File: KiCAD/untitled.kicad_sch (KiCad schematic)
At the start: 71 parts, among them J1 Power, J10 Conn_01x04, J11 Conn_01x04, J12 FDCAN_1, J13 FDCAN_2, J5 Debug Header, J6 Conn_01x04, J7 Conn_01x04, J8 Conn_01x04, J9 Conn_01x04, Q6 AO3400A, Q7 AO3400A, Q8 AO3400A, SW1 PTS810SJM250SMTRLFS, SW2 PTS810SJM250SMTRLFS, SW3 PTS810SJM250SMTRLFS, SW4 PTS810SJM250SMTRLFS, SW5 SMQS-02R-TP, U1 STM32H573RIT6, U12 TPS7A2033DQNR, U5 USBLC6-2SC6, U7 MCP2562FD-E/P, U8 MCP2562FD-E/P, X1 SC-32S32.768kHz20PPM7pF, Y2 ECS-80-18-23B-JTM-TR

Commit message: Sync KiCAD project
Forgot to push this earlier
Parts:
- C11: LCSC Part (none) -> C19666
- C12, C13, C14, C15, C17, C26, C27, C30, C8: LCSC Part (none) -> C1525
- C16: LCSC Part (none) -> C15849
- C22: LCSC Part (none) -> C440198
- C23, C28, C29: LCSC Part (none) -> C307331
- C24: LCSC Part (none) -> C52923
- C25: LCSC Part (none) -> C23630
- D5: LCSC Part (none) -> C2297
- D6: LCSC Part (none) -> C2296
- R14, R15, R24, R26, R28: LCSC Part (none) -> C25744
- R16, R17: LCSC Part (none) -> C25905
- R18: LCSC Part (none) -> C22775
- R19: LCSC Part (none) -> C22962
- R20, R21: LCSC Part (none) -> C8218
- R22: LCSC Part (none) -> C22787
- R23, R25, R27: LCSC Part (none) -> C25091
- R30, R31: LCSC Part (none) -> C17909
- U1: LCSC Part (none) -> C22371377
- U5: LCSC Part (none) -> C7519

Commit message: Fix all DRC errors
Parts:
- USBC1: footprint easyeda2kicad:USB-C_SMD-TYPE-C-31-M-12_1 -> Connector_USB:USB_C_Receptacle_HRO_TYPE-C-31-M-12
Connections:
- net GND: now also Y2.4
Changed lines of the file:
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@@
 (kicad_sch
-	(version 20250114)
+	(version 20260306)
 	(generator "eeschema")
-	(generator_version "9.0")
+	(generator_version "10.0")
 	(paper "A4")
 	(title_block

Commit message: Oscillator Test Pads + Re-Fix USB-C
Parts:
- added TP5: LSE, TestPoint:TestPoint_Pad_2.0x2.0mm, symbol Connector:TestPoint_Alt
- added TP7: HSE, TestPoint:TestPoint_Pad_2.0x2.0mm, symbol Connector:TestPoint_Alt
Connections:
- net GND: now also USBC1.2 (SH), USBC1.3 (SH), USBC1.4 (SH), USBC1.A1 (GND), USBC1.A12 (GND), USBC1.B1 (GND), USBC1.B12 (GND), USBC1.SH; no longer USBC1.A1B12 (GND), USBC1.B1A12 (GND)
- net HSE_IN: now also TP7.1
- net LSE_IN: now also TP5.1
- net USB_VBUS: now also USBC1.A4 (VBUS), USBC1.A9 (VBUS), USBC1.B4 (VBUS), USBC1.B9 (VBUS); no longer USBC1.A4B9 (VBUS), USBC1.B4A9 (VBUS)
- no-connect marks 6 -> 2
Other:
- moved on the sheet: USBC1

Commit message: USB-C Schematic Changes
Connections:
- net GND: no longer USBC1.2 (SH), USBC1.3 (SH), USBC1.4 (SH)

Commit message: Change some TPs to 2.54mm pin headers, silkscreen changes, start led redo
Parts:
- added D10: SK6812MINI-E, LED_SMD:LED_SK6812MINI-E_3.2x2.8mm_P1.5mm_ReverseMount, symbol LED:SK6812MINI-E

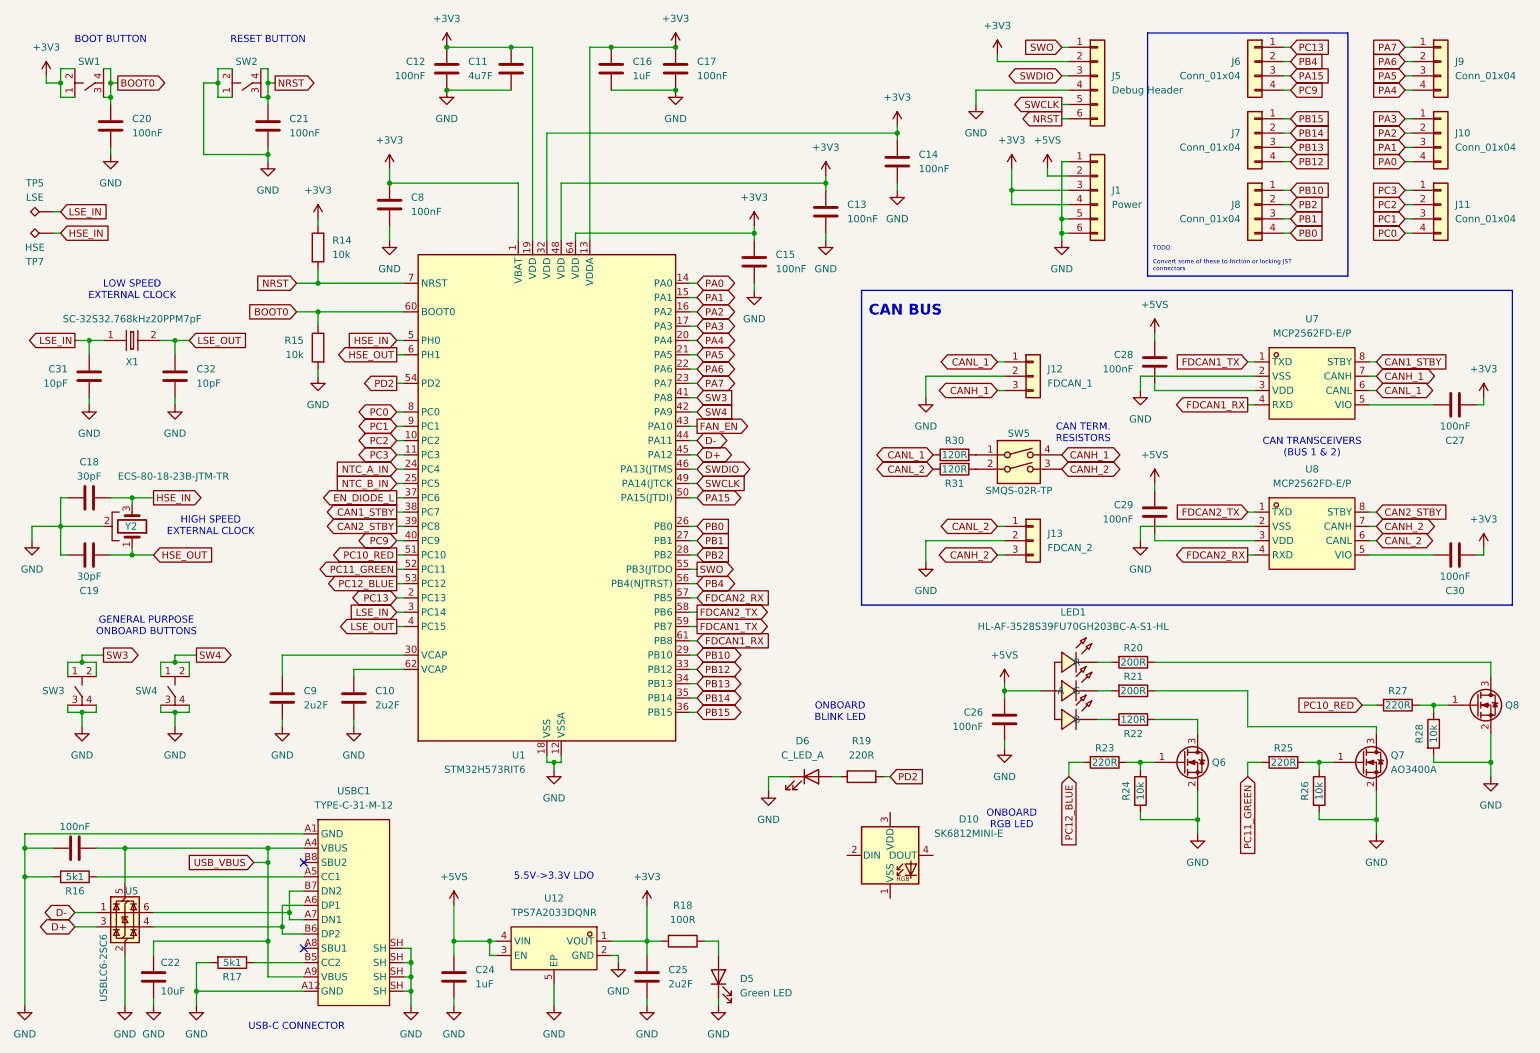
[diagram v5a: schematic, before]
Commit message: Replace RGB LED with cheaper SK6812 LEDs, expose freed UART pins
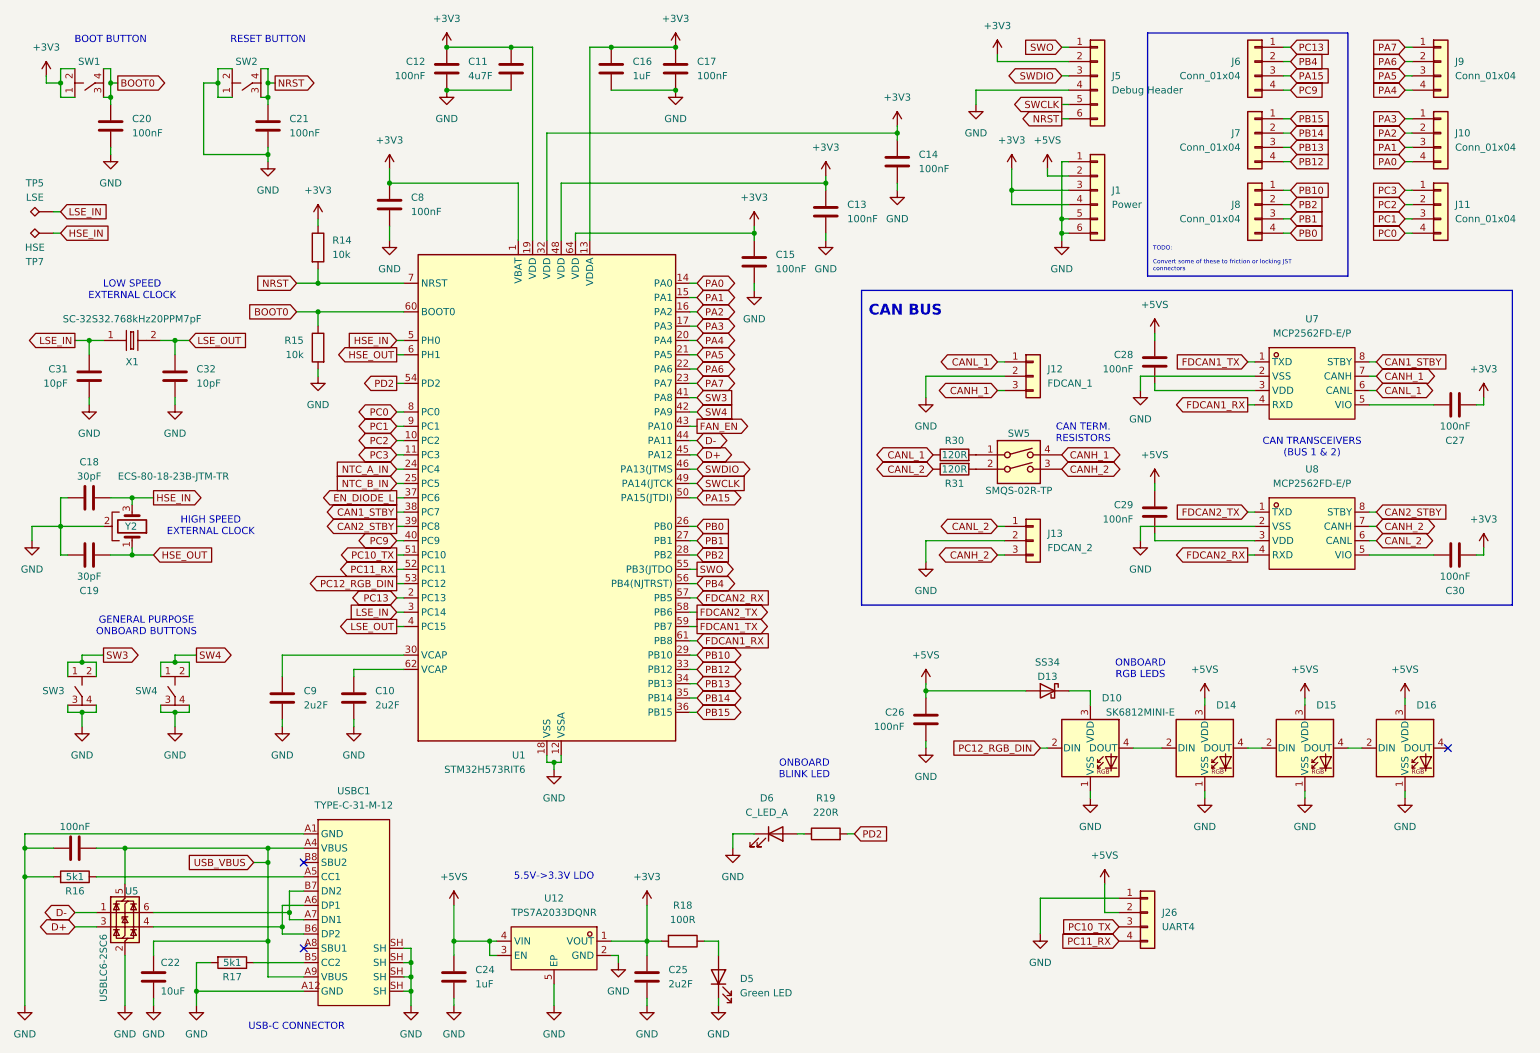
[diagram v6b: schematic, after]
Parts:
- removed LED1: HL-AF-3528S39FU70GH203BC-A-S1-HL, easyeda2kicad:LED-SMD_4P-L3.2-W2.7-TL_HL-AF-3528S39FU70GH20, symbol easyeda2kicad:HL-AF-3528S39FU70GH203BC-A-S1-HL
- removed Q6, Q7, Q8: AO3400A, Package_TO_SOT_SMD:SOT-23, symbol Transistor_FET:AO3400A
- removed R20, R21: 200R, Resistor_SMD:R_0603_1608Metric, symbol Device:R
- removed R22: 120R, Resistor_SMD:R_0603_1608Metric, symbol Device:R
- removed R23, R25, R27: 220R, Resistor_SMD:R_0402_1005Metric, symbol Device:R
- removed R24, R26, R28: 10k, Resistor_SMD:R_0402_1005Metric, symbol Device:R
- added D13: SS34, Diode_SMD:D_SMA, symbol Device:D_Schottky
- added D14, D15, D16: SK6812MINI-E, LED_SMD:LED_SK6812MINI-E_3.2x2.8mm_P1.5mm_ReverseMount, symbol LED:SK6812MINI-E
- added J26: UART4, Connector_PinHeader_2.54mm:PinHeader_1x04_P2.54mm_Vertical, symbol Connector_Generic:Conn_01x04
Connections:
- net PC12_BLUE is gone; now on net PC12_RGB_DIN: U1.53 (PC12)
- net +5VS: now also D13.2 (A), D14.3 (VDD), D15.3 (VDD), D16.3 (VDD), J26.2 (Pin_2)
- net GND: now also D10.1 (VSS), D14.1 (VSS), D15.1 (VSS), D16.1 (VSS), J26.1 (Pin_1)
- net PC12_RGB_DIN: now reaches D10.2 (DIN)
- net at D10.3 (VDD): now also D13.1 (K)
- net at D10.4 (DOUT): now also D14.2 (DIN)
- net PC10_RED renamed PC10_TX
- net PC10_TX: now also J26.3 (Pin_3)
- net PC11_GREEN renamed PC11_RX
- net PC11_RX: now also J26.4 (Pin_4)
- new net: D14.4 (DOUT), D15.2 (DIN)
- new net: D15.4 (DOUT), D16.2 (DIN)
- no-connect marks 2 -> 3
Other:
- note added: "ONBOARD RGB LEDS"
- note removed: "ONBOARD RGB LED"
- moved on the sheet: C26, D10, D6, R19

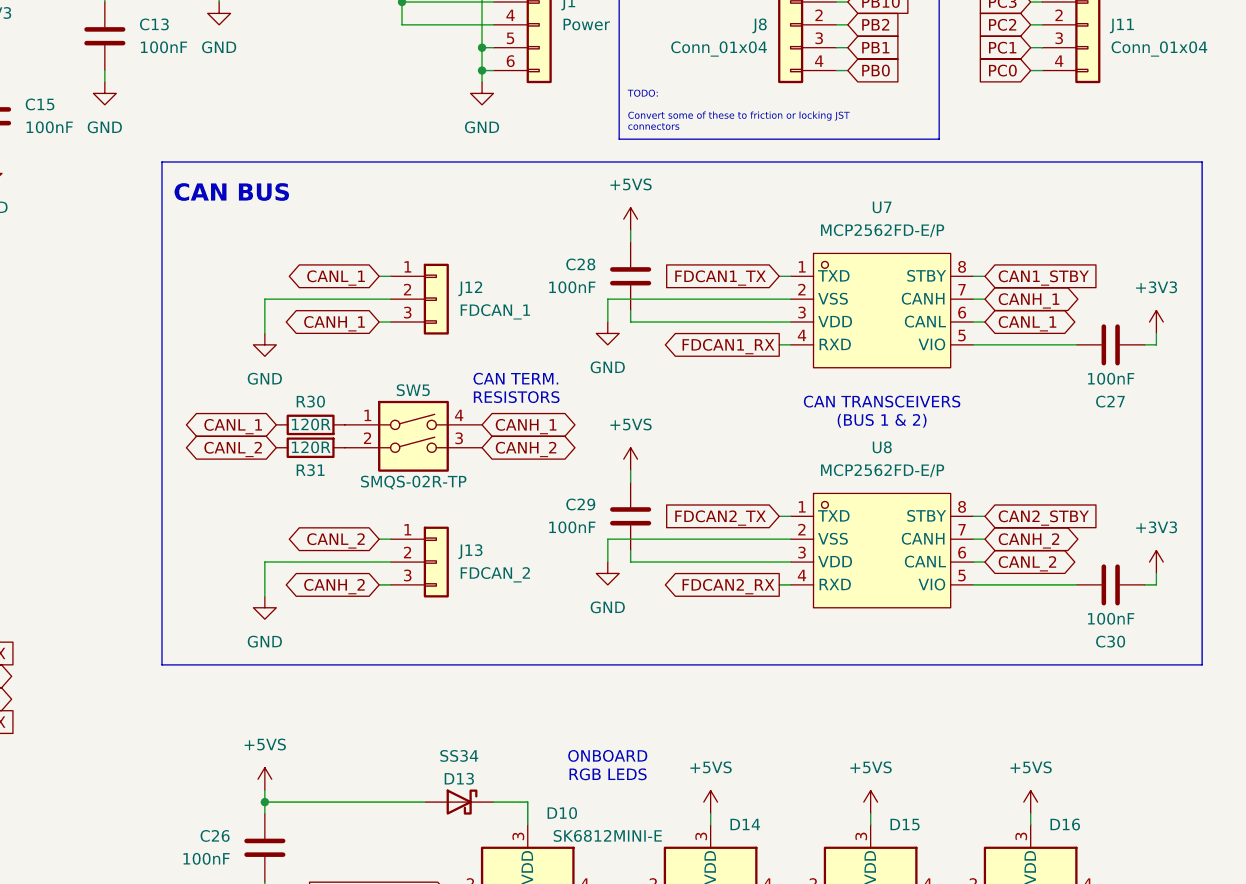
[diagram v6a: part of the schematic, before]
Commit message: Fixed silly miswired CAN transceivers
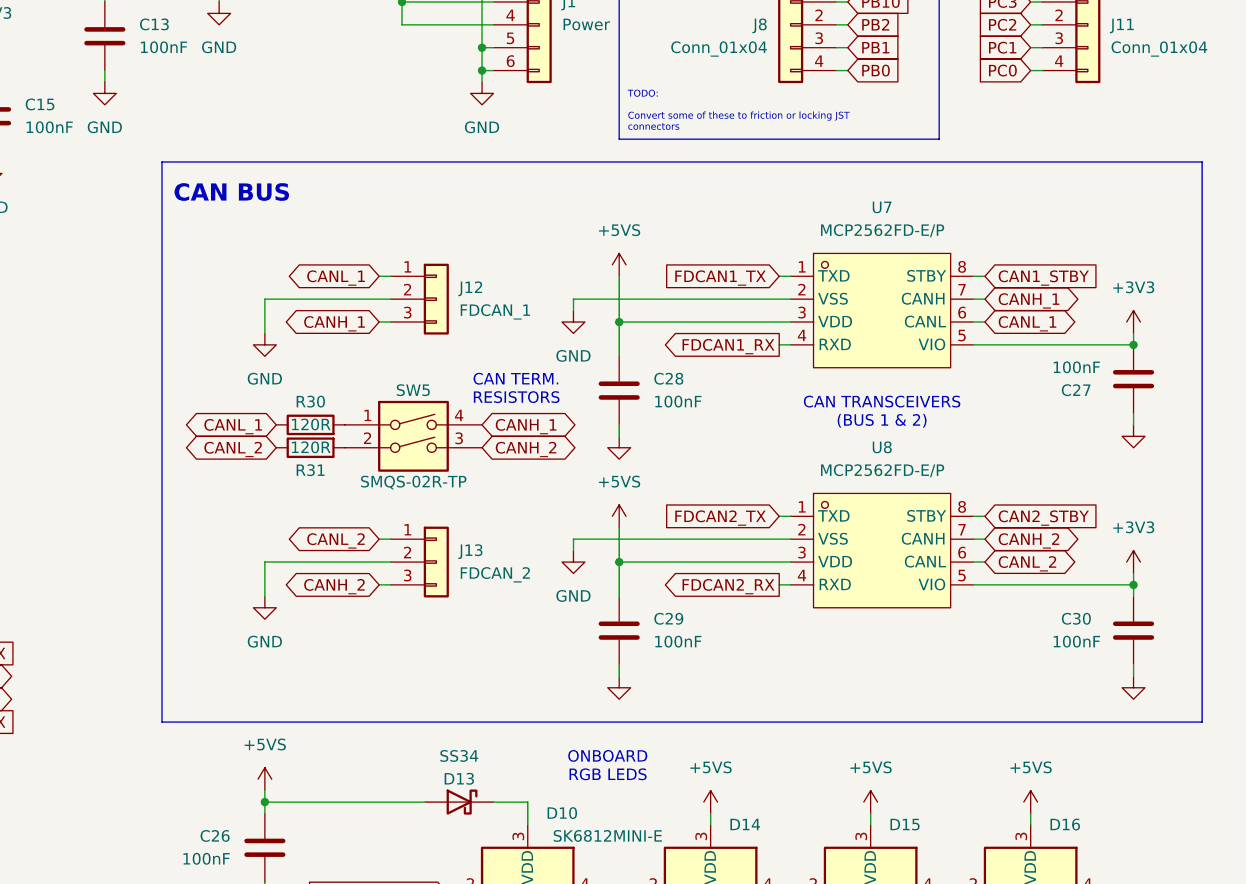
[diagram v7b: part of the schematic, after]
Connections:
- net +3V3: now also U7.5 (VIO), U8.5 (VIO)
- net +5VS: now also C29.2, U7.3 (VDD), U8.3 (VDD); no longer C29.1
- net GND: now also C27.2, C28.2, C29.1, C30.2
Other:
- moved on the sheet: C27, C28, C29, C30

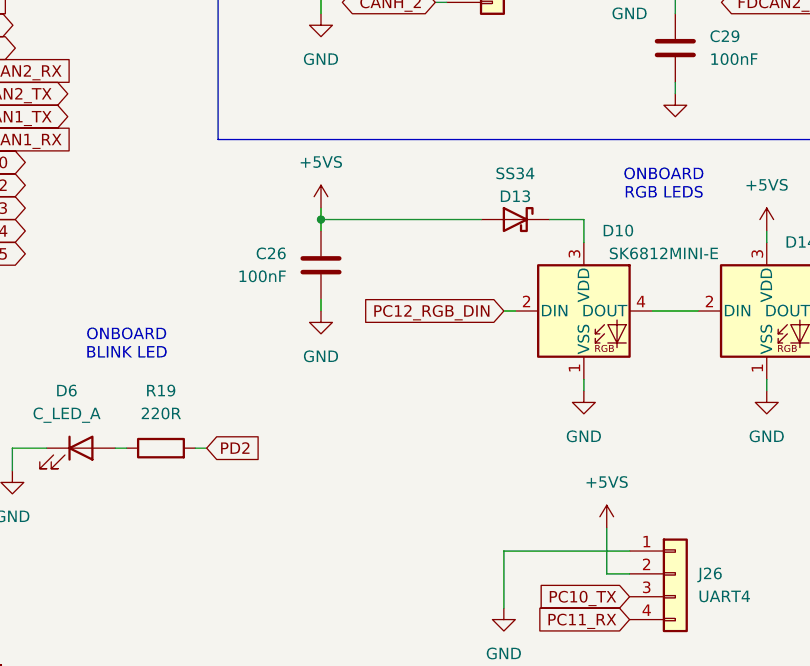
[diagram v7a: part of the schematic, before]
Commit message: Finish SK7812 layouts + new forward mount footprint from reverse extended leads footprint
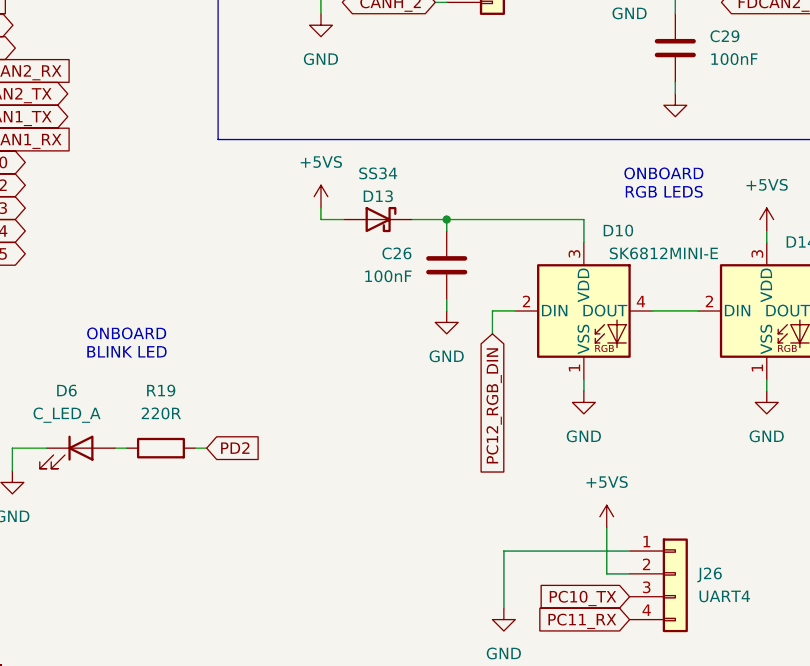
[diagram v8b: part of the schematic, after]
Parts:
- D10, D14, D15, D16: footprint LED_SMD:LED_SK6812MINI-E_3.2x2.8mm_P1.5mm_ReverseMount -> LED_SMD:LED_SK6812MINI-E_3.2x2.8mm_P1.5mm
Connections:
- net +5VS: no longer C26.1
- net at D10.3 (VDD), D13.1 (K): now also C26.1
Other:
- moved on the sheet: C26, D13
